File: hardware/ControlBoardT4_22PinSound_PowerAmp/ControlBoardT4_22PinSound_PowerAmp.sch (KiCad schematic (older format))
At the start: 17 parts, among them J1 RC, J10 Conn_01x02_Male, J11 LinAct_M3, J12 Conn_01x04_Male, J13 Main Power, J2 LinAct, J3 SpeedCtrl, J4 Power Input, J5 I2C, J6 Left_M1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

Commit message: Added space to allow for JST Connectors
JST connectors are 2.54 pitch.
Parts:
- J1: footprint Connector_PinHeader_2.54mm:PinHeader_1x04_P2.54mm_Vertical -> Useful Modifications:JST_XH_B4B-XH-A_1x04_P2.54mm_Vertical
- J2, J3: footprint Connector_PinHeader_2.54mm:PinHeader_1x03_P2.54mm_Vertical -> Useful Modifications:JST_XH_B3B-XH-A_1x03_P2.54mm_Vertical
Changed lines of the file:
@@
 F 0 "J1" H 4580 4950 50  0000 R CNN
 F 1 "RC" H 4430 4950 50  0000 R CNN
-F 2 "Connector_PinHeader_2.54mm:PinHeader_1x04_P2.54mm_Vertical" H 4380 4700 50  0001 C CNN
+F 2 "Useful Modifications:JST_XH_B4B-XH-A_1x04_P2.54mm_Vertical" H 4380 4700 50  0001 C CNN
 F 3 "~" H 4380 4700 50  0001 C CNN
 	1    4380 4700
@@
 F 0 "J3" H 2280 3620 50  0000 R CNN
 F 1 "SpeedCtrl" H 2130 3620 50  0000 R CNN
-F 2 "Connector_PinHeader_2.54mm:PinHeader_1x03_P2.54mm_Vertical" H 1980 3370 50  0001 C CNN
+F 2 "Useful Modifications:JST_XH_B3B-XH-A_1x03_P2.54mm_Vertical" H 1980 3370 50  0001 C CNN
 F 3 "~" H 1980 3370 50  0001 C CNN
 	1    1980 3370
@@
 F 0 "J2" H 2180 2970 50  0000 R CNN
 F 1 "LinAct" H 2030 2970 50  0000 R CNN
-F 2 "Connector_PinHeader_2.54mm:PinHeader_1x03_P2.54mm_Vertical" H 1880 2720 50  0001 C CNN
+F 2 "Useful Modifications:JST_XH_B3B-XH-A_1x03_P2.54mm_Vertical" H 1880 2720 50  0001 C CNN
 F 3 "~" H 1880 2720 50  0001 C CNN
 	1    1880 2720

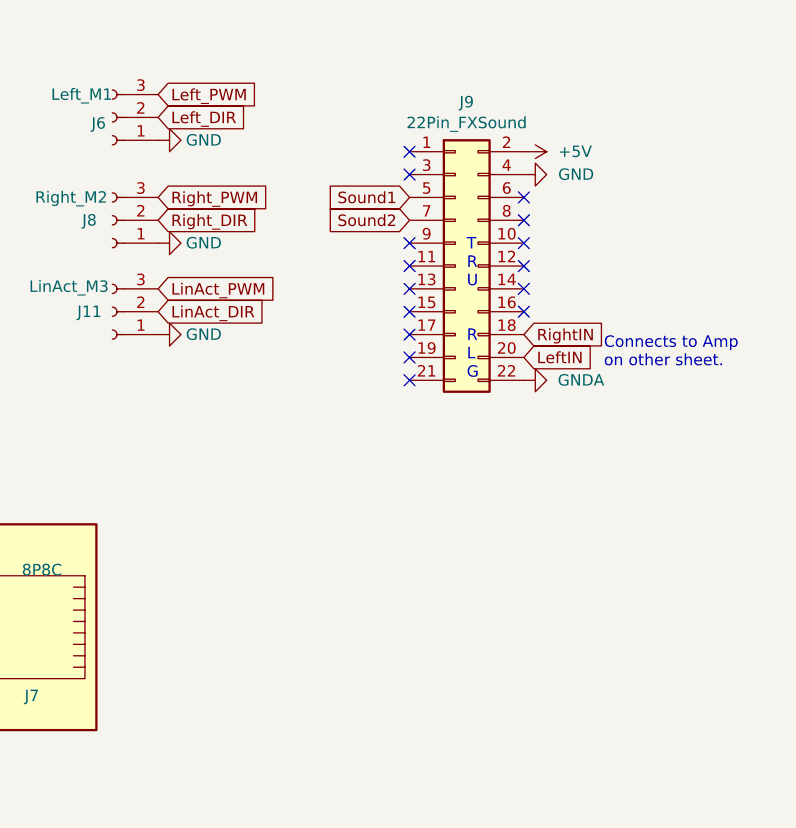
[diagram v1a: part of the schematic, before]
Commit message: adding additional sound headers to primary Teensy 4 PCB
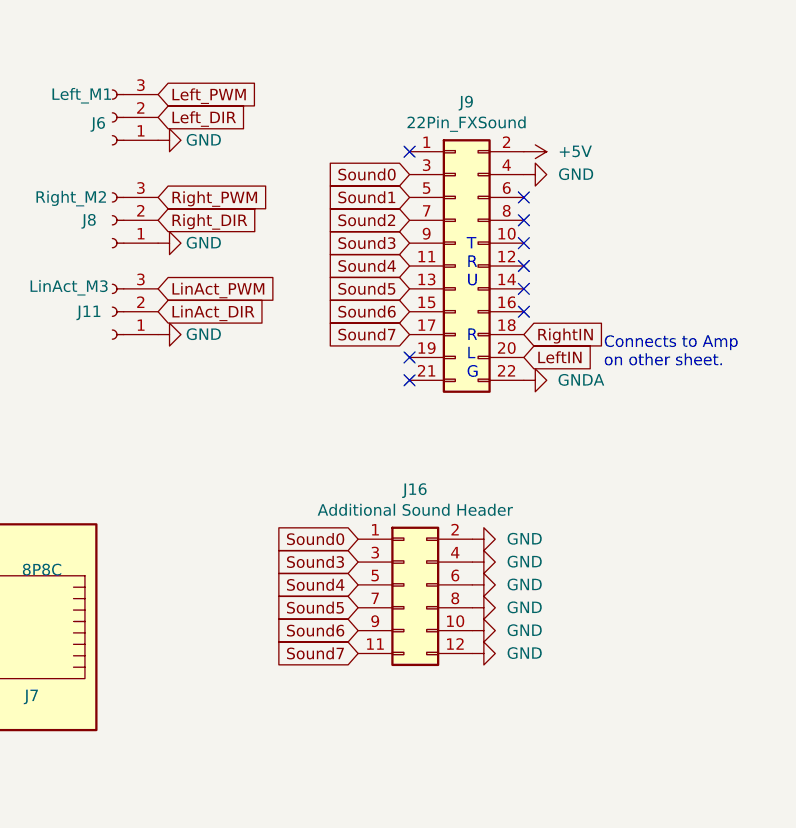
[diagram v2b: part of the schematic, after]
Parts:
- added J16: Additional Sound Header, Connector_PinSocket_2.54mm:PinSocket_2x06_P2.54mm_Vertical, symbol Connector_Generic:Conn_02x06_Odd_Even
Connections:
- net GND: now also J16.10 (Pin_10), J16.12 (Pin_12), J16.2 (Pin_2), J16.4 (Pin_4), J16.6 (Pin_6), J16.8 (Pin_8)
- net Sound4: now reaches J9.11 (Pin_11)
- net Sound4: now also J16.5 (Pin_5)
- net Sound5: now reaches J9.13 (Pin_13)
- net Sound5: now also J16.7 (Pin_7)
- net Sound6: now reaches J9.15 (Pin_15)
- net Sound6: now also J16.9 (Pin_9)
- net Sound7: now reaches J9.17 (Pin_17)
- net Sound7: now also J16.11 (Pin_11)
- net Sound0: now reaches J9.3 (Pin_3)
- net Sound0: now also J16.1 (Pin_1)
- net Sound3: now reaches J9.9 (Pin_9)
- net Sound3: now also J16.3 (Pin_3)
- no-connect marks 22 -> 16
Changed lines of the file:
@@
 	0    1    1    0
 $EndComp
-NoConn ~ 8990 3530
-NoConn ~ 8990 3430
-NoConn ~ 8990 3330
 NoConn ~ 8990 2830
-NoConn ~ 8990 3630
 NoConn ~ 8990 3730
 NoConn ~ 8990 3830
-NoConn ~ 8990 2930
-NoConn ~ 8990 3230
 NoConn ~ 9490 3030
 Text Notes 9240 3430 0    50   ~ 0
@@
 TxA6
 NoConn ~ 3840 3470
+Text GLabel 8990 2930 0    50   Input ~ 0
+Sound0
+Text GLabel 8990 3230 0    50   Input ~ 0
+Sound3
+Text GLabel 8990 3330 0    50   Input ~ 0
+Sound4
+Text GLabel 8990 3430 0    50   Input ~ 0
+Sound5
+Text GLabel 8990 3530 0    50   Input ~ 0
+Sound6
+Text GLabel 8990 3630 0    50   Input ~ 0
+Sound7
+$Comp
+L Connector_Generic:Conn_02x06_Odd_Even J16
+U 1 1 6251B752
+P 8965 4725
+F 0 "J16" H 9015 5142 50  0000 C CNN
+F 1 "Additional Sound Header" H 9015 5051 50  0000 C CNN
+F 2 "Connector_PinSocket_2.54mm:PinSocket_2x06_P2.54mm_Vertical" H 8965 4725 50  0001 C CNN
+F 3 "~" H 8965 4725 50  0001 C CNN
+	1    8965 4725
+	1    0    0    -1
+$EndComp
+Text GLabel 8765 4525 0    50   Input ~ 0
+Sound0
+Text GLabel 8765 4625 0    50   Input ~ 0
+Sound3
+Text GLabel 8765 4725 0    50   Input ~ 0
+Sound4
+Text GLabel 8765 4825 0    50   Input ~ 0
+Sound5
+Text GLabel 8765 4925 0    50   Input ~ 0
+Sound6
+Text GLabel 8765 5025 0    50   Input ~ 0
+Sound7
+$Comp
+L power:GND #PWR017
+U 1 1 6251E13E
+P 9265 4525
+F 0 "#PWR017" H 9265 4275 50  0001 C CNN
+F 1 "GND" V 9265 4375 50  0000 R CNN
+F 2 "" H 9265 4525 50  0001 C CNN
+F 3 "" H 9265 4525 50  0001 C CNN
+	1    9265 4525
+	0    -1   -1   0
+$EndComp
+$Comp
+L power:GND #PWR018
+U 1 1 6251EF8C
+P 9265 4625
+F 0 "#PWR018" H 9265 4375 50  0001 C CNN
+F 1 "GND" V 9265 4475 50  0000 R CNN
+F 2 "" H 9265 4625 50  0001 C CNN
+F 3 "" H 9265 4625 50  0001 C CNN
+	1    9265 4625
+	0    -1   -1   0
+$EndComp
+$Comp
+L power:GND #PWR020
+U 1 1 6251F484
+P 9265 4725
+F 0 "#PWR020" H 9265 4475 50  0001 C CNN
+F 1 "GND" V 9265 4575 50  0000 R CNN
+F 2 "" H 9265 4725 50  0001 C CNN
+F 3 "" H 9265 4725 50  0001 C CNN
+	1    9265 4725
+	0    -1   -1   0
+$EndComp
+$Comp
+L power:GND #PWR021
+U 1 1 6251F903
+P 9265 4825
+F 0 "#PWR021" H 9265 4575 50  0001 C CNN
+F 1 "GND" V 9265 4675 50  0000 R CNN
+F 2 "" H 9265 4825 50  0001 C CNN
+F 3 "" H 9265 4825 50  0001 C CNN
+	1    9265 4825
+	0    -1   -1   0
+$EndComp
+$Comp
+L power:GND #PWR022
+U 1 1 6251FD7F
+P 9265 4925
+F 0 "#PWR022" H 9265 4675 50  0001 C CNN
+F 1 "GND" V 9265 4775 50  0000 R CNN
+F 2 "" H 9265 4925 50  0001 C CNN
+F 3 "" H 9265 4925 50  0001 C CNN
+	1    9265 4925
+	0    -1   -1   0
+$EndComp
+$Comp
+L power:GND #PWR023
+U 1 1 6252010C
+P 9265 5025
+F 0 "#PWR023" H 9265 4775 50  0001 C CNN
+F 1 "GND" V 9265 4875 50  0000 R CNN
+F 2 "" H 9265 5025 50  0001 C CNN
+F 3 "" H 9265 5025 50  0001 C CNN
+	1    9265 5025
+	0    -1   -1   0
+$EndComp
 $EndSCHEMATC
